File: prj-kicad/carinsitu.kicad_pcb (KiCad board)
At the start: 4 copper layers, 130 x 50 mm, 65 parts, among them P1 BAT, P2 MOT, P3 CONN_3, P4 CONN_1, P5 CONN_4, SW1 SWITCH_SLIDE, U1 ESP8285, U2 MIC2860, U3 MAX17205, U4 SN74LVC1T45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

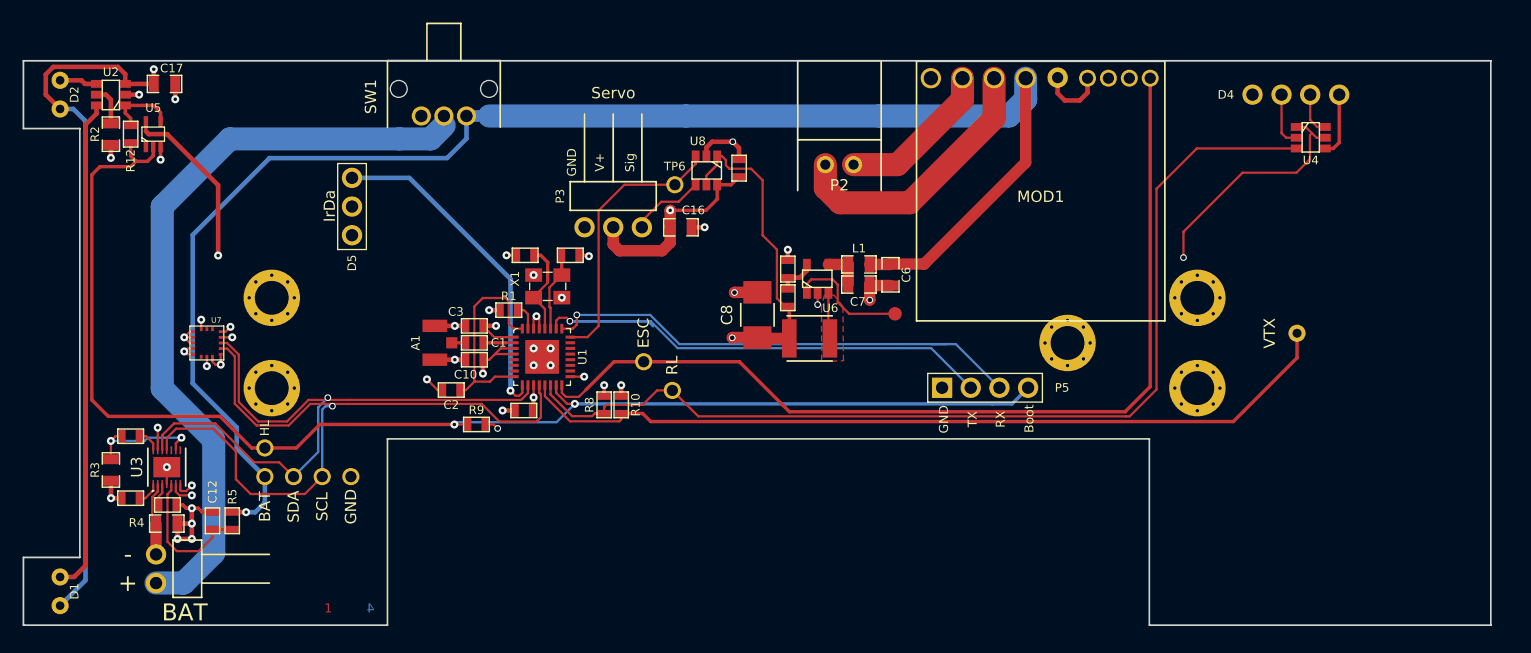
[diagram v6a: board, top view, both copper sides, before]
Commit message: Move components listed in TODO
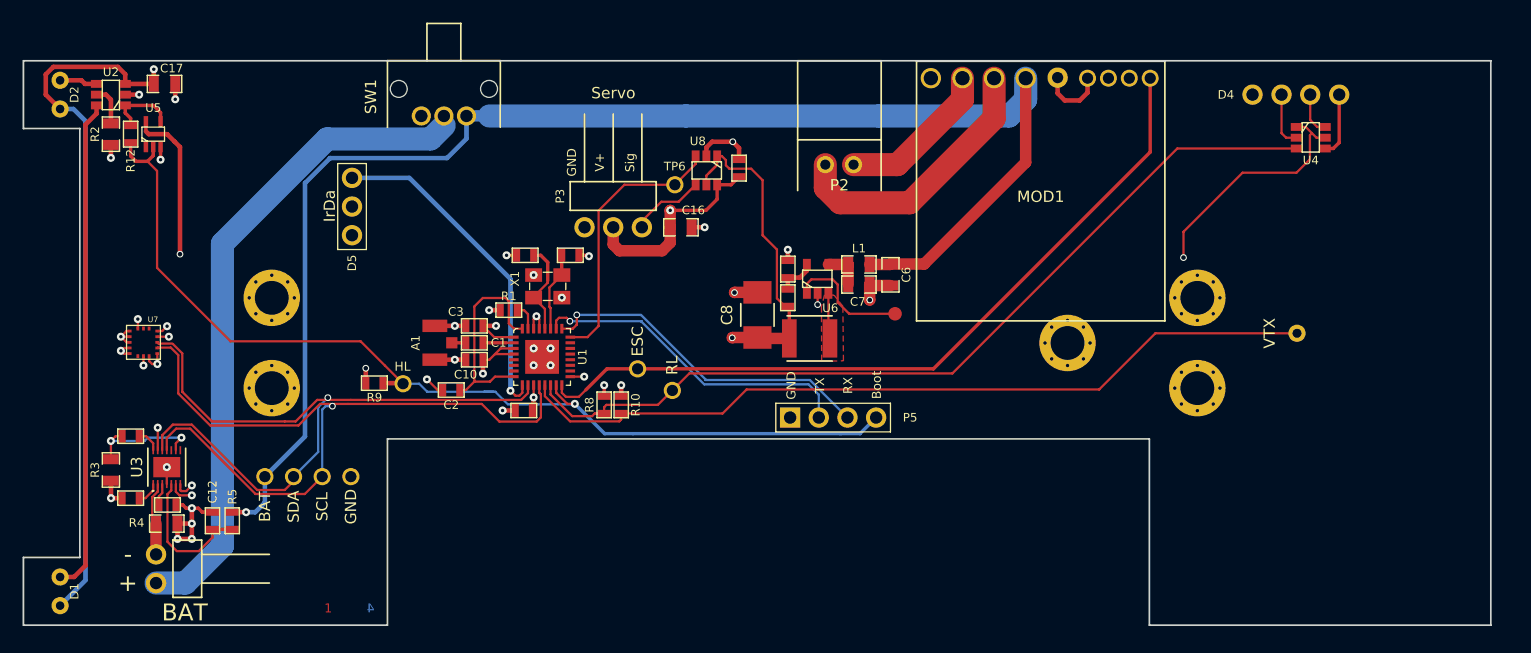
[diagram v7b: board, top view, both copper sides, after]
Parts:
- moved P5 13.7 mm to (154.5, 111.6)
- moved TP8 13.5 mm to (116.4, 108.6)
- moved R9 9.75 mm to (113.8, 108.6), turned to 0 degrees
- moved U7 5.62 mm to (93.4, 104.9)
- moved TP7 0.83 mm to (137.2, 107.3)
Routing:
- net HL_PWM: track 119.6 -> 89.9 mm, vias 2 -> 1
- net U0_TX: track 47.7 -> 29.0 mm
- net PPM_ESC: track 84.3 -> 68.5 mm
- net U0_RX: track 43.9 -> 30.1 mm
- net RL_DAT: track 90.2 -> 77.9 mm
- net GND: track 427.9 -> 439.1 mm
- net Net-(P1-Pad1): track 67.6 -> 58.9 mm
- net +VBAT: track 136.5 -> 128.0 mm
- net SDA: track 58.1 -> 64.3 mm
- net +3V3: track 215.8 -> 220.9 mm
- net SCL: track 65.0 -> 68.7 mm
- net VTX: track 73.9 -> 72.1 mm

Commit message: Do the remaining TODO list
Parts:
- added SW2: Reset, Button_Switch_SMD:SW_Push_1P1T_NO_6x6mm_H9.5mm, F.Cu at (121.0, 93.0)
- added TP10: CONN_1, carinsitu:TP, F.Cu at (109.2, 122.7)
- added TP11: CONN_1, carinsitu:TP, F.Cu at (111.7, 122.7)
- P4: value CONN_1 -> CONN_3; footprint carinsitu:TP -> carinsitu:CONN_61300311021
- moved P4 23.9 mm to (206.7, 83.0)
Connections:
- P4 pad 1: VTX -> +5V
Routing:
- net +5V: track 201.9 -> 239.1 mm
- net GND: track 439.1 -> 471.8 mm
- net VTX: track 72.1 -> 93.1 mm
- net Net-(C2-Pad1): track 18.8 -> 33.0 mm
- net +3V3: track 220.9 -> 234.0 mm, vias 12 -> 13
- net PPM_ESC: track 68.5 -> 66.2 mm
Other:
- board text added: "+5V"
- board text added: "3V3"
